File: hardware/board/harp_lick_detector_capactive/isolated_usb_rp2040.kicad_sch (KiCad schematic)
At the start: 47 parts, among them J2 Conn_01x03_Male, J4 AudioJack3, J5 USB_C_Receptacle_USB2.0, SW1 SW_Push, U2 TPD2EUSB30, U3 ADUM4160, U4 RP2040, U5 W25Q128JVS, X1 ECS-TXO-2016

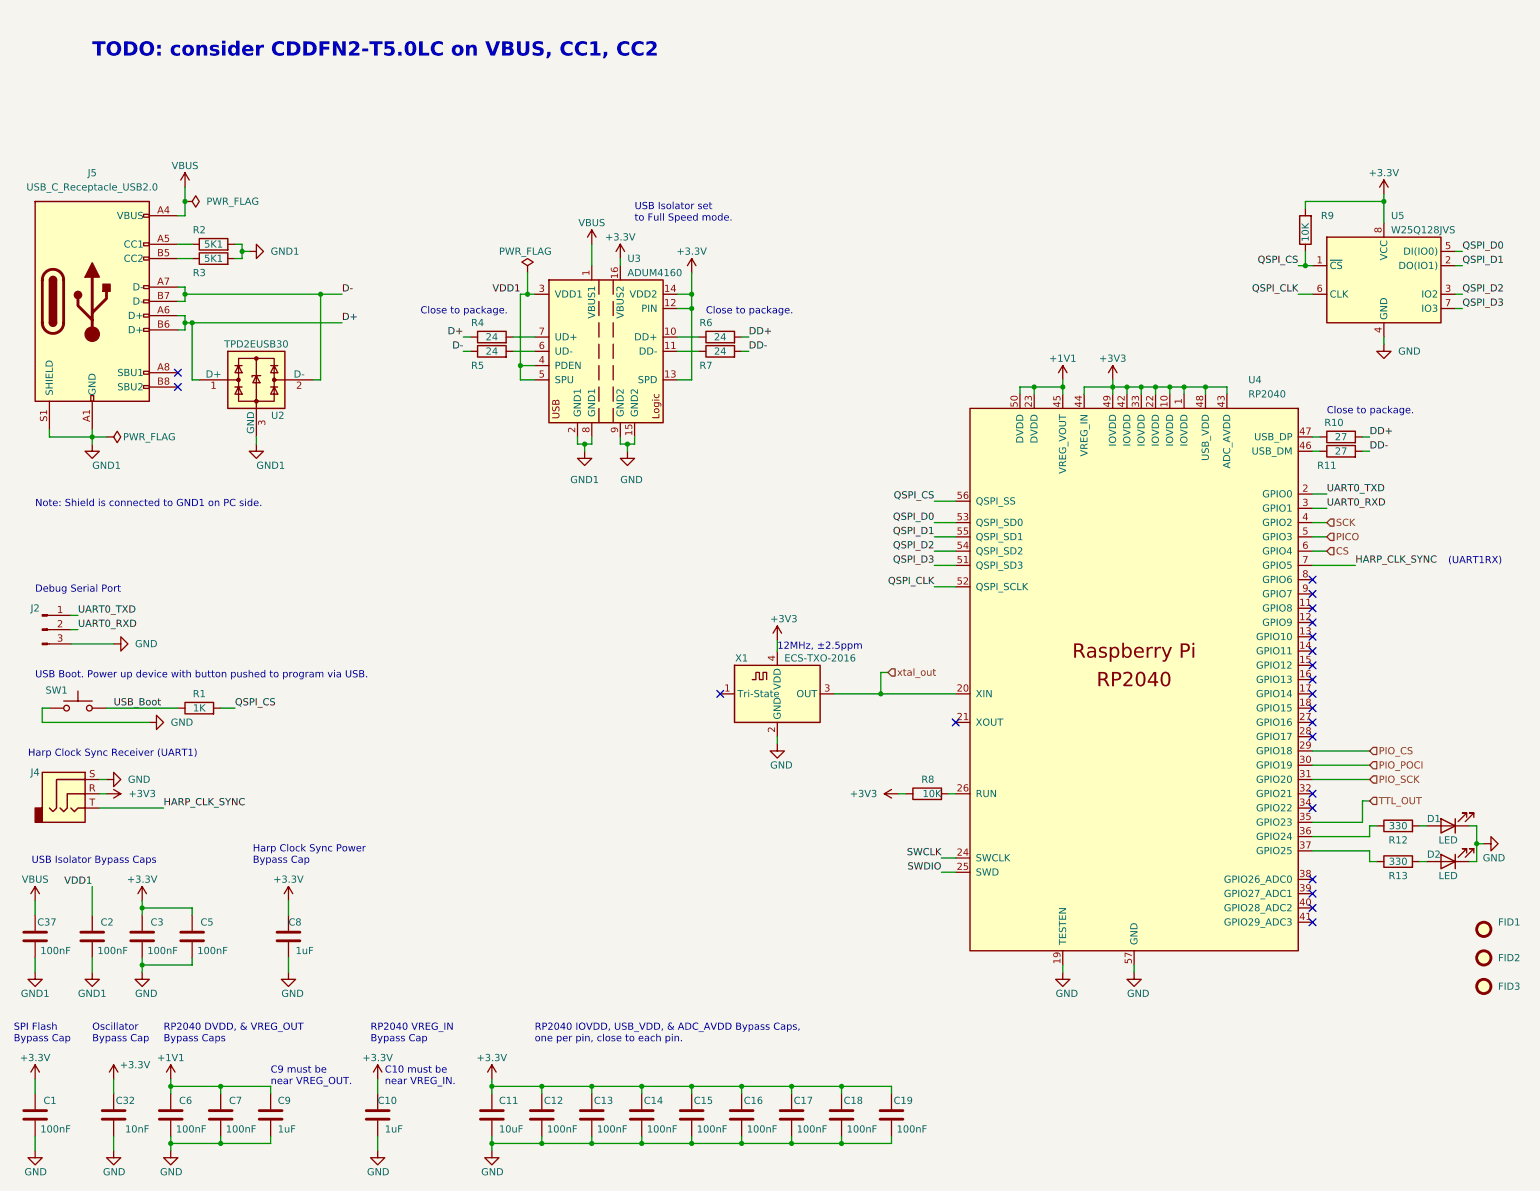
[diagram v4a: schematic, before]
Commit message: add tvs diodes; remove run pullup; finish trace guard
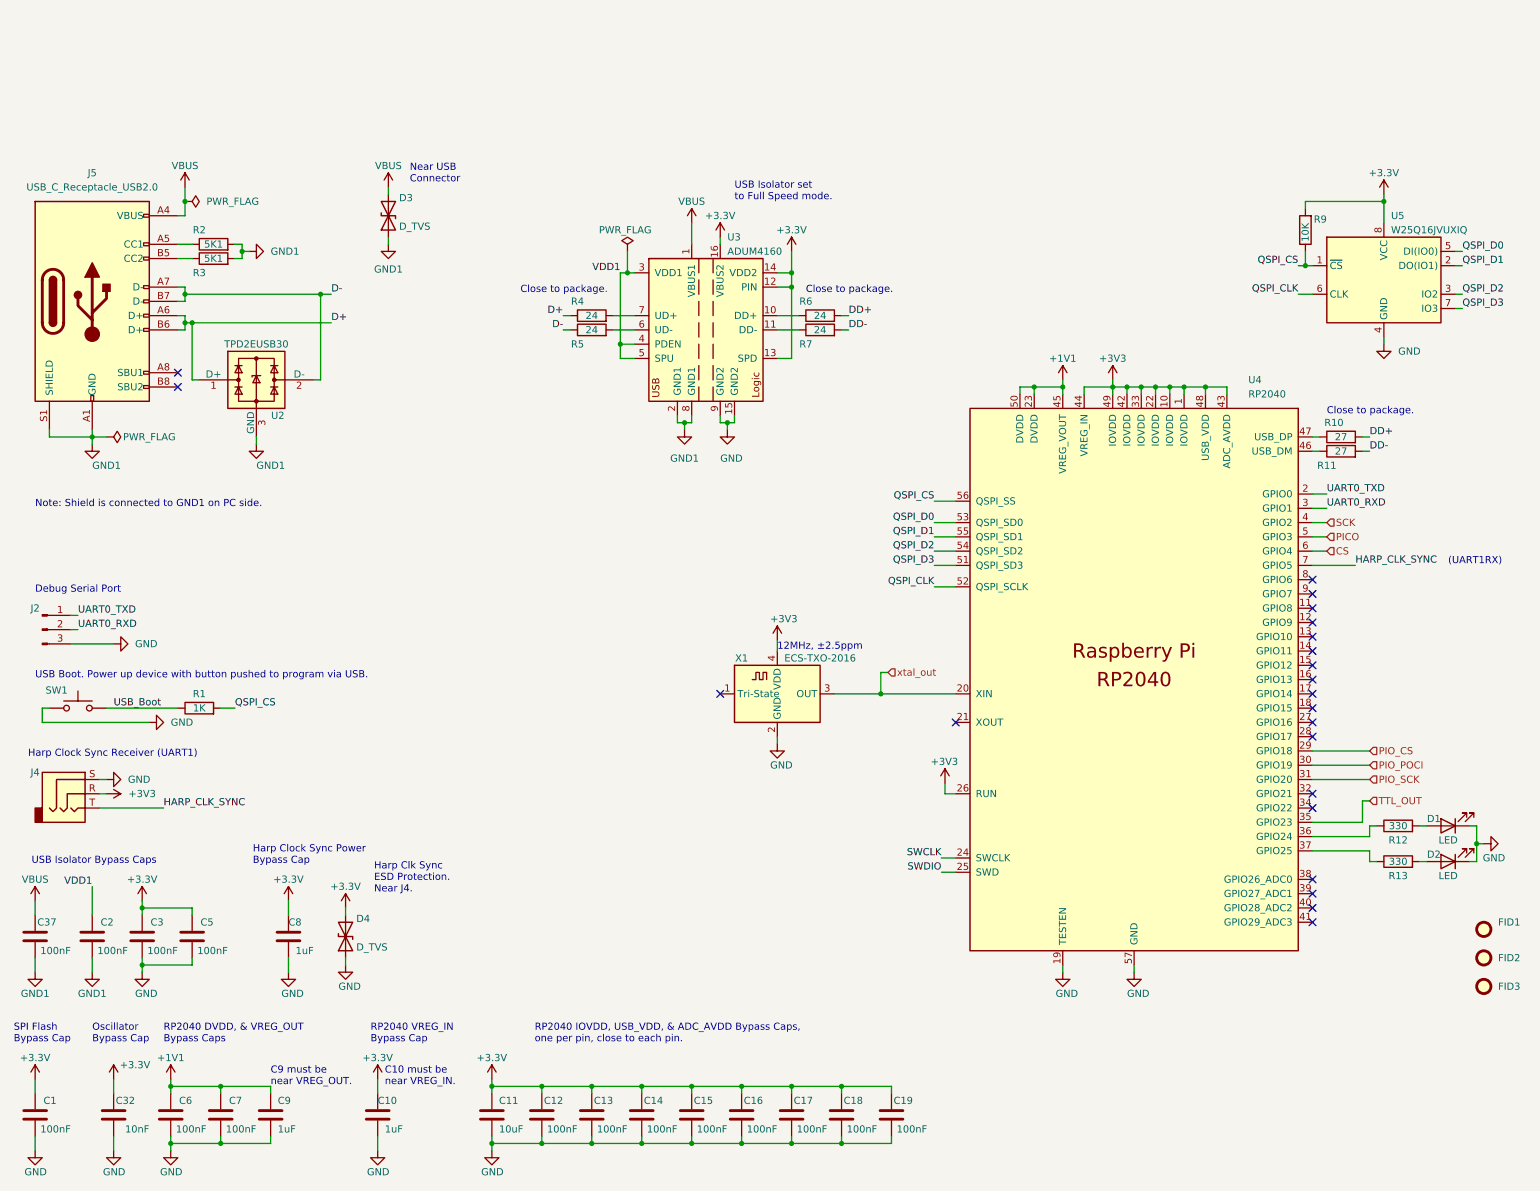
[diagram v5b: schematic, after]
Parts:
- removed R8: 10K, Resistor_SMD:R_0402_1005Metric, symbol Device:R
- added D3, D4: D_TVS, Diode_SMD:D_0402_1005Metric, symbol Device:D_TVS
- R9: Notes (none) -> DNP
- U5: value W25Q128JVS -> W25Q16JVUXIQ; footprint Package_SO:SOIC-8_5.23x5.23mm_P1.27mm -> kicad_component_library:Winbond-8USON-2x3mm; Link https://www.digikey.com/en/products/detail/winbond-electronics/W25Q128JVSIQ-TR/5803944 -> https://www.digikey.com/en/products/detail/winbond-electronics/W25Q16JVUXIQ-TR/15182017; Manufacturer Number W25Q128JVSIQ TR -> W25Q16JVUXIQ TR; PCBWay Link https://www.pcbway.com/components/detail/W25Q128JVSIQTR/436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 -> https://www.pcbway.com/components
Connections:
- net +3V3: now also U4.26 (RUN), D4.2 (A2)
- net GND: now also D4.1 (A1)
- net GND1: now also D3.1 (A1)
- net VBUS: now also D3.2 (A2)
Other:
- note added: "Harp Clk Sync ESD Protection. Near J4."
- note added: "Near USB Connector"
- note removed: "TODO: consider CDDFN2-T5.0LC on VBUS, CC1, CC2"
- moved on the sheet: R4, R5, R6, R7, U3

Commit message: update ads7049 pinout
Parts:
- added C56: 1uF, Capacitor_SMD:C_0402_1005Metric, symbol Device:C
- R2, R3: footprint Resistor_SMD:R_0603_1608Metric_Pad0.98x0.95mm_HandSolder -> Resistor_SMD:R_0402_1005Metric; Link https://www.digikey.com/en/products/detail/panasonic-electr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 -> https://www.digikey.com/en/products/detail/yageo/RT0402FRE0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; Manufacturer Panasonic Electronic Components -> Yageo; Manufacturer Number ERJ-UP3F5101V -> RT0402FRE075K1L; PCBWay Link https://www.pcbway.com/components/detail/ERJUP3F5101V/56444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 -> https://www.pcbway.com/components/detail/RT0402FRE075K1L/44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
- SW1: Manufacturer (none) -> Omron Electronics Inc-EMC Div; Manufacturer Number (none) -> B3U-1000P
- U3: Manufacturer (none) -> Analog Devices Inc.
- X1: PCBWay Link (none) -> https://www.pcbway.com/components/detail/ECSTXO201633120TR/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
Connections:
- net GND1: now also C56.2
- net VBUS: now also C56.1
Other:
- moved on the sheet: C2, C3, C37, C5, C8, D4, J2, J4, R1, SW1

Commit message: draft v0.6.0 board
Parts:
- removed R12, R13: 330, Resistor_SMD:R_0402_1005Metric, symbol Device:R
- removed SW1: SW_Push, Button_Switch_SMD:SW_SPST_B3U-1000P, symbol Switch:SW_Push
- added R11 (x2): 680, Resistor_SMD:R_0402_1005Metric, symbol Device:R
- added SW1: ~, kicad_component_library:SW_Push_1P1T-SH_NO_Vertical_Wuerth_WS-TASV, symbol kicad_component_library:SW_Push_with_gnd
- J4: Manufacturer (none) -> CUI Devices
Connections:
- net GND: now also SW1.4, SW1.SH
- net USB_Boot: now also SW1.2
- net at D2.2 (A): now also R11.2
- net at U4.36 (GPIO24): now also R11.1
- net at U4.37 (GPIO25): now also R11.1
- net at D1.2 (A): now also R11.2
- net CS: no longer names the net of U4.6 (GPIO4)
- net PICO: no longer names the net of U4.5 (GPIO3)
- net SCK renamed 100KHZ_SQ_WAVE_OUT
- net SWCLK: no longer names the net of U4.24 (SWCLK)
- net SWDIO: no longer names the net of U4.25 (SWD)
- net xtal_out: no longer names the net of U4.20 (XIN), X1.3 (OUT)
- no-connect marks 22 -> 28
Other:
- moved on the sheet: C56, J2, R1

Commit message: make r0.6 board snapshot
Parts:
- C11: Alternate (none) -> CL21B106KOQNNNE
- R9: Notes DNP -> (none)
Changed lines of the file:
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@@
       (effects (font (size 1.27 1.27)) hide)
     )
-    (property "Notes" "DNP" (at 243.84 27.305 0)
+    (property "Notes" "" (at 243.84 27.305 0)
       (effects (font (size 1.27 1.27)) hide)
     )
@@
       (effects (font (size 1.27 1.27)) hide)
     )
+    (property "Alternate" "CL21B106KOQNNNE" (at 99.06 184.785 0)
+      (effects (font (size 1.27 1.27)) hide)
+    )
